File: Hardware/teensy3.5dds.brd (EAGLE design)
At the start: 95.8 x 84.1 mm, 97 parts, among them IC1 AD8034, IC2 AD8034, IC3 AD8034, IC5 AD8034, IC6 AD737KRZ-R7, IC7 AD8034, IC8 AD8034, J1 1776275-2, J2 1776275-2, Q1 10MHz, U1 TEENSY_3.5/3.6_BASIC, U2 ATMEGA32U4-AU, X1 1-227161-0

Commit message: fixes following the advice of people better than me at making PCBs
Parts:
- moved R12 32.3 mm to (49.0, 75.2), turned to 0 degrees
- moved R9 30.7 mm to (48.5, 68.8)
- moved R6 30.1 mm to (49.0, 72.9)
- moved R5 27.7 mm to (43.7, 71.1), turned to 0 degrees
- moved IC1 22.6 mm to (56.4, 72.1)
- moved C1 21.3 mm to (54.6, 77.5)
- moved C2 18.3 mm to (55.1, 68.1), turned to 180 degrees
- moved R11 17.8 mm to (62.5, 73.8), turned to 90 degrees
- moved R13 15.5 mm to (69.0, 78.9), turned to 0 degrees
- moved J_DAC0_OUT 13.6 mm to (53.8, 64.0)
- moved R20 13.5 mm to (63.0, 58.7)
- moved C5 12.7 mm to (68.6, 86.4), turned to 0 degrees
- moved R32 11.3 mm to (63.0, 64.0)
- moved R18 10.5 mm to (45.7, 55.0)
- moved C10 10.5 mm to (52.6, 51.7)
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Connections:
- removed net V-1: R13.1
- net DAC0: now also IC1.5; no longer IC1.3
- net DAC0_OFFSET: now also IC1.1; no longer IC1.7
- net N$21: now also IC1.2; no longer IC1.6
- net N$23: now also IC1.6, IC1.7; no longer IC1.1, IC1.2
- net N$26: now also IC1.3; no longer IC1.5
- net V-: now also R13.1
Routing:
- net V+: track 0.00 -> 409.1 mm, vias 0 -> 15
- net V-: track 68.7 -> 294.1 mm, vias 7 -> 4
- net DAC0_OFFSET: track 83.6 -> 35.0 mm
- net DAC0_SEL: track 70.8 -> 95.1 mm
- net DAC0_OUT: track 0.00 -> 24.0 mm
- net DAC0: track 30.5 -> 49.1 mm
- net SQUARE_SEL: track 120.8 -> 103.6 mm
- net +5V: track 71.3 -> 87.8 mm, vias 4 -> 6
- net N$26: track 12.0 -> 26.5 mm, vias 0 -> 2
- net N$20: track 0.00 -> 13.5 mm
- net N$24: track 3.43 -> 14.9 mm
- net N$14: track 16.1 -> 5.98 mm
- net N$23: track 11.5 -> 4.79 mm
- net SQUARE: track 44.6 -> 38.2 mm
- net N$19: track 40.6 -> 35.3 mm
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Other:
- board size 95.8 x 84.1 mm -> 90 x 84.5 mm

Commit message: board v1.0
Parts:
- removed C30, C34: 100p, rcl:C0805
- removed C32: 10p, rcl:C0805
- removed IC8: AD8034, linear:SO08
- removed J_DAC0_OUT, J_SQUARE_OUT: (no value), con-lstb:MA03-1
- removed J_DISPLAY: (no value), con-lstb:MA04-1
- removed J_SPI: (no value), con-lstb:MA03-2
- removed R43: (no value), rcl:R0805
- removed U$5: (no value), holes:3,0
- added C11, C12: 100n, rcl:C0805
- added C26: 100p, rcl:C0805
- added IC4: AD8034, linear:SO08
- added JDAC0_OUT, JSQUARE_OUT: (no value), con-lstb:MA03-1
- added JDISPLAY: (no value), con-lstb:MA04-1
- added JSPI: (no value), con-lstb:MA03-2
- added R19: 1k, rcl:R0805
- added R21: 787, rcl:M0805
- added R23: 10k, Potentiometer_vertical:MA03-1
- added U$1: (no value), holes:3,0
- C1: value 100n -> 1u; device rcl:C0805 -> rcl:C1206
- C19: device rcl:C1206 -> rcl:C0805
- C22: value 100n -> 10p
- C23: value 1u -> 150p
- C25: value (none) -> 1p
- C27: value 100p -> 10p
- C28: value 10p -> 100p
- C3: value 1u -> 22p; device rcl:C1206 -> rcl:C0805
- C4: value 100n -> 22p
- C5: device rcl:C0805 -> rcl:C1206
- C7: value 22p -> 1u
- C8: value 22p -> 100n
- IC5: value AD8034 -> AD737KRZ-R7; device linear:SO08 -> AD737KRZ-R7:SOIC127P600X175-8N
- IC6: value AD737KRZ-R7 -> AD8034; device AD737KRZ-R7:SOIC127P600X175-8N -> linear:SO08
- Q1: value 10MHz -> 16MHz
- R12: value 1k -> 500; device rcl:R0805 -> rcl:M0805
- R13: value 100k -> 500; device rcl:RTRIM3296W -> rcl:M0805
- R15: value (none) -> 2.74k
- R16: value (none) -> 100k; device rcl:M0805 -> rcl:RTRIM3296W
- R17: value (none) -> 1k; device rcl:M0805 -> rcl:R0805
- R18: value 2.74k -> 1k
- R20: value 787 -> 1k; device rcl:M0805 -> rcl:R0805
- R22: value 14.3k -> 1k; device rcl:M0805 -> rcl:R0805
- R25: value 10k -> 1.5k; device Potentiometer_vertical:MA03-1 -> rcl:R0805
- R26: value (none) -> 14.3k; device rcl:R0805 -> rcl:M0805
- R27, R42: value (none) -> 50
- R28, R37: value (none) -> 5k
- R30, R41: value (none) -> 1k
- R31: value 10k -> 2k; device Potentiometer_vertical:MA03-1 -> rcl:M0805
- R32: value 562 -> 10k; device rcl:R0805 -> Potentiometer_vertical:MA03-1
- R33: value 243 -> 10k
- R34: value 20k -> 562
- R35: value 1.78k -> (none); device rcl:M0805 -> rcl:R0805
- R36: value (none) -> 20k
- R38: value (none) -> 10k
- R39: value (none) -> 14.3k
- R4, R9: value 1k -> 10k
- R40: value 50 -> (none)
- R5: value 100k -> 10k; device rcl:RTRIM3296W -> rcl:R0805
- R6: value 1k -> 100k; device rcl:R0805 -> rcl:RTRIM3296W
- RL1, RL2: value PRME_15005SOCKET -> PRME_15005NOSOCKET; device prme15005:DIL14_SOCKET -> prme15005:DIL14
- moved R15 89.0 mm to (2.92, 59.8), turned to 0 degrees
- moved J2 86.6 mm to (84.6, 92.7)
- moved J1 80.3 mm to (84.6, 81.8)
- moved R41 79.2 mm to (78.7, 54.9), turned to 180 degrees
- moved R10 78.9 mm to (3.05, 71.4)
- moved C13 78.4 mm to (2.92, 55.2), turned to 0 degrees
- moved X1 77.2 mm to (7.37, 46.2)
- moved R1 74.2 mm to (86.2, 54.3)
- moved LED1 74.1 mm to (85.5, 52.0)
- moved R8 73.8 mm to (3.05, 69.2), turned to 0 degrees
- moved C19 72.5 mm to (67.9, 45.1), turned to 0 degrees
- moved S1 71.3 mm to (79.9, 40.4)
- moved R35 70.9 mm to (17.0, 49.5), turned to 0 degrees
- moved C18 67.0 mm to (78.7, 59.7), turned to 0 degrees
- moved R7 66.7 mm to (16.5, 72.6)
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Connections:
- removed net N$20: R13.2, R4.1
- new net N$36: IC6.2, R35.2, R40.1
- new net N$37: IC7.6, R16.2, R18.1
- net +5V: now also C1.1, C2.1, C5.1, C7.1, JDISPLAY.3, JSPI.5, R4.1, R5.1; no longer C19.1, C22.1, C23.1, C3.1, J_DISPLAY.3, J_SPI.5, R41.1, R42.1
- net AMPL_MEASURE: now also IC4.7, R41.2, U2.37; no longer IC5.7, R39.2, U2.38
- net DAC0_FILTERED: now also C28.1, JDAC0_OUT.1; no longer C34.1, J_DAC0_OUT.1
- net DAC0_OFFSET: now also JDAC0_OUT.3, R11.1; no longer J_DAC0_OUT.3, R12.1
- net DAC0_OUT: now also JDAC0_OUT.2; no longer J_DAC0_OUT.2
- net DAC0_SEL: now also R13.1, U1.22/A8; no longer R17.1, U1.36/A17
- net GND: now also C10.2, C11.1, C12.2, C13.1, C14.2, C15.1, C16.2, C17.1, C18.2, C19.1, C2.2, C22.1, C27.1, C3.1, C4.1, C5.2, C7.2, C8.2, C9.1, IC5.3, IC5.8, JDISPLAY.4, JSPI.1, R10.2, R19.2, R9.1; no longer C10.1, C13.2, C14.1, C15.2, C16.1, C17.2, C18.1, C19.2, C2.1, C22.2, C23.2, C28.1, C3.2, C32.1, C4.2, C5.1, C7.1, C8.1, C9.2, IC6.8, IC7.6, J_DISPLAY.4, J_SPI.1, R43.1, R6.2, R8.2
- net INTERRUPT: now also U1.21/A7, U2.22; no longer U1.37/A18, U2.25
- net MISO: now also JSPI.3; no longer J_SPI.3
- net MOSI: now also JSPI.6; no longer J_SPI.6
- net N$1: now also R31.2, R33.1; no longer R33.2, R35.1
- net N$10: now also R22.1; no longer R24.1
- net N$11: now also IC4.2; no longer IC5.2
- net N$13: now also IC4.3, R24.1, R25.2; no longer IC5.3, R26.1, R27.2
- net N$14: now also IC5.6, R37.1; no longer IC6.6, R36.1
- net N$15: now also R32.1; no longer R31.1
- net N$16: now also IC4.6, R37.2, R41.1; no longer IC5.6, R36.2, R39.1
- net N$17: now also R12.2; no longer R16.2
- net N$18: now also R13.2; no longer R17.2
- net N$19: now also IC6.1, R40.2, R42.1; no longer IC8.1, IC8.2, R40.1
- net N$21: now also R10.1, R11.2; no longer R12.2, R6.1
- net N$22: now also IC4.5, R38.2, R39.1; no longer IC5.5, R37.2, R38.1
- net N$23: now also R7.1; no longer R11.1
- net N$24: now also R19.1, R20.2; no longer R10.2, R8.1
- net N$25: now also R4.2, U2.40; no longer R41.2, U2.32
- net N$26: now also R7.2, R8.2; no longer R11.2, R9.2
- net N$27: now also R17.1; no longer R7.1
- net N$28: now also R17.2, R18.2; no longer R4.2, R7.2
- net N$29: now also R9.2, U2.39; no longer R43.2, U2.30
- net N$3: now also IC6.5, R23.2; no longer IC8.5, R25.2
- net N$31: now also C3.2; no longer C7.2
- net N$34: now also R27.1, R31.1; no longer R15.1, R33.1
- net N$4: now also C4.2; no longer C8.2
- net N$5: now also IC6.6, R22.2; no longer IC8.6, R24.2
- net N$50: now also C23.2, R15.1; no longer C27.2, R18.1
- net N$53: now also C23.1, R21.1; no longer C27.1, R20.1
- net N$56: now also R6.2, R8.1; no longer R5.2, R9.1
- net N$58: now also C22.2, R15.2; no longer C24.2, R18.2
- net N$6: now also R42.2; no longer R40.2
- net N$61: now also C26.1, R21.2, R26.1; no longer C30.1, R20.2, R22.1
- net N$62: now also C26.2, R34.1; no longer C30.2, R32.1
- net N$63: now also C24.2, R26.2; no longer C28.2, R22.2
- net N$73: now also C28.2, R34.2, R36.1; no longer C34.2, R32.2, R34.1
- net N$75: now also C27.2, R36.2; no longer C32.2, R34.2
- net N$8: now also R5.2, U2.41; no longer R42.2, U2.31
- net N$9: now also IC5.2, IC6.7, R32.2, R32.3, R35.1; no longer IC6.2, IC8.3, IC8.7, R31.2, R31.3
- net OFF_MEASURE: now also IC4.1, U2.36; no longer IC5.1, U2.37
- net RX1: now also U1.1/TX; no longer U1.32/A13
- net SCK: now also JSPI.4; no longer J_SPI.4
- net SCL: now also JDISPLAY.1; no longer J_DISPLAY.1
- net SDA: now also JDISPLAY.2; no longer J_DISPLAY.2
- net SQUARE: now also U1.A22/DAC1; no longer U1.39/A20
- net SQUARE_FILTERED: now also JSQUARE_OUT.1, R33.2; no longer J_SQUARE_OUT.1, R35.2
- net SQUARE_OFFSET: now also JSQUARE_OUT.3, R20.1, R27.2; no longer J_SQUARE_OUT.3, R10.1, R15.2
- net SQUARE_OUT: now also JSQUARE_OUT.2; no longer J_SQUARE_OUT.2
- net SQUARE_SEL: now also R12.1, U1.23/A9; no longer R16.1, U1.35/A16
- net SS: now also JSPI.2; no longer J_SPI.2
- net TX1: now also U1.0/RX; no longer U1.31/A12
- net V+: now also C10.1, C12.1, C14.1, C16.1, C18.1, C8.1, IC4.8, IC5.7, IC6.8, R16.3, R23.3, R24.2, R38.1, R6.3; no longer C1.1, C13.1, C15.1, C17.1, C4.1, C9.1, IC5.8, IC6.7, IC8.8, R13.3, R25.3, R26.2, R37.1, R5.3
- net V-: now also C11.2, C13.2, C15.2, C17.2, C19.2, C9.2, IC4.4, IC5.5, R16.1, R23.1, R39.2, R6.1; no longer C10.2, C14.2, C16.2, C18.2, C2.2, C5.2, IC6.5, IC8.4, R13.1, R27.1, R38.2, R5.1
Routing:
- net SQUARE_SEL: track 103.6 -> 20.4 mm
- net V-: track 294.1 -> 372.0 mm, vias 4 -> 7
- net DAC0_SEL: track 95.1 -> 40.3 mm, vias 1 -> 3
- net INTERRUPT: track 77.7 -> 27.4 mm
- net V+: track 409.1 -> 447.7 mm, vias 15 -> 11
- net +5V: track 87.8 -> 50.2 mm, vias 6 -> 11
- net N$14: track 5.98 -> 41.1 mm, vias 0 -> 2
- net N$37: track 0.00 -> 34.9 mm, vias 0 -> 2
- net AMPL_MEASURE: track 47.2 -> 15.7 mm, vias 2 -> 0
- net DAC0: track 49.1 -> 18.6 mm
- net DAC0_OFFSET: track 35.0 -> 65.4 mm, vias 2 -> 1
- net SQUARE_OFFSET: track 58.6 -> 29.2 mm, vias 1 -> 0
- net N$9: track 65.4 -> 39.0 mm
- net N$10: track 16.5 -> 41.7 mm, vias 0 -> 1
- net N$8: track 68.9 -> 44.5 mm
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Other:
- board size 90 x 84.5 mm -> 90.4 x 63.4 mm
- board text added: "vcc"

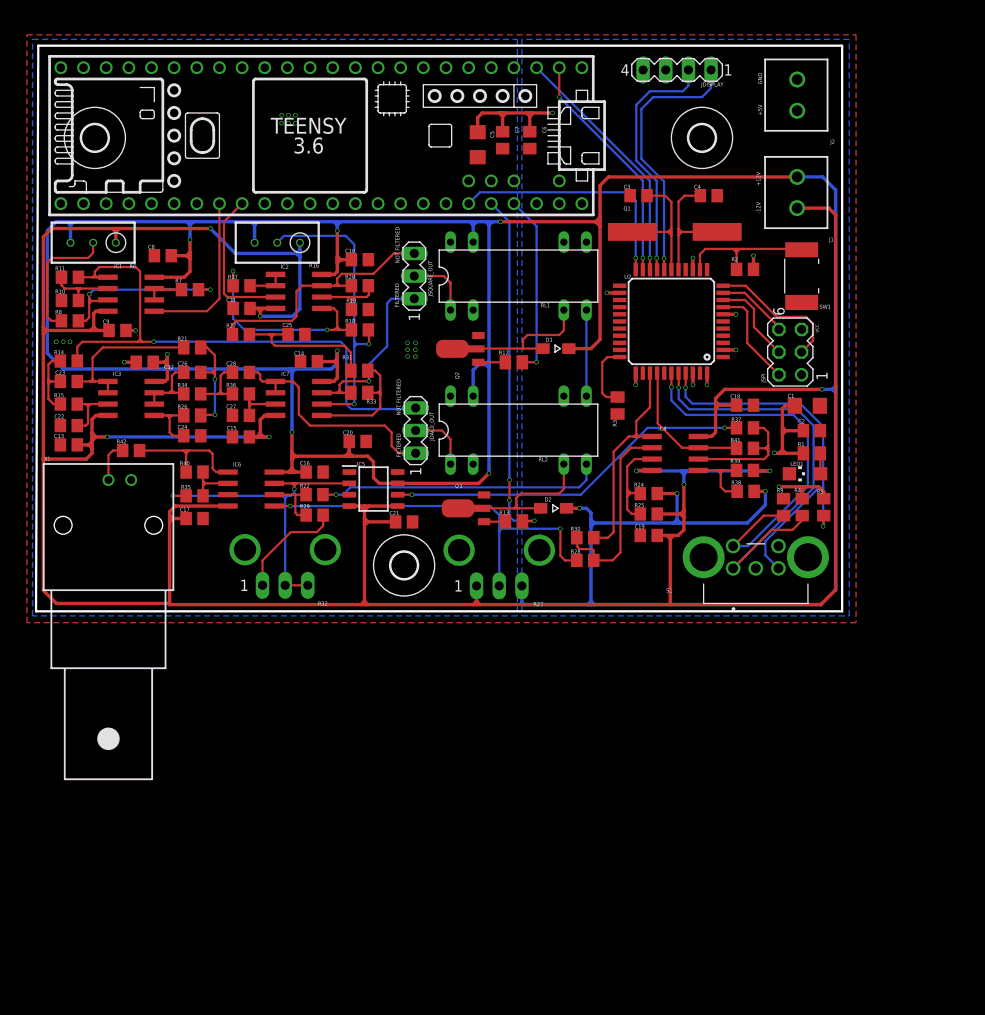
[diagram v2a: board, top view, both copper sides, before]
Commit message: hardware: board v2.0
correct a few derps with missing resistors
correct encoder pushbutton
add i2c pullup resistors
move some 32u4 pins to more accessible ones, supported by the arduino micro bootloader
wire the 5v led to the builtin led on 32u4
remove the ad737, move the a non-inverting summer circuit (wave+offset) with a peak finder to get the peak of the wave no matter the offset condition
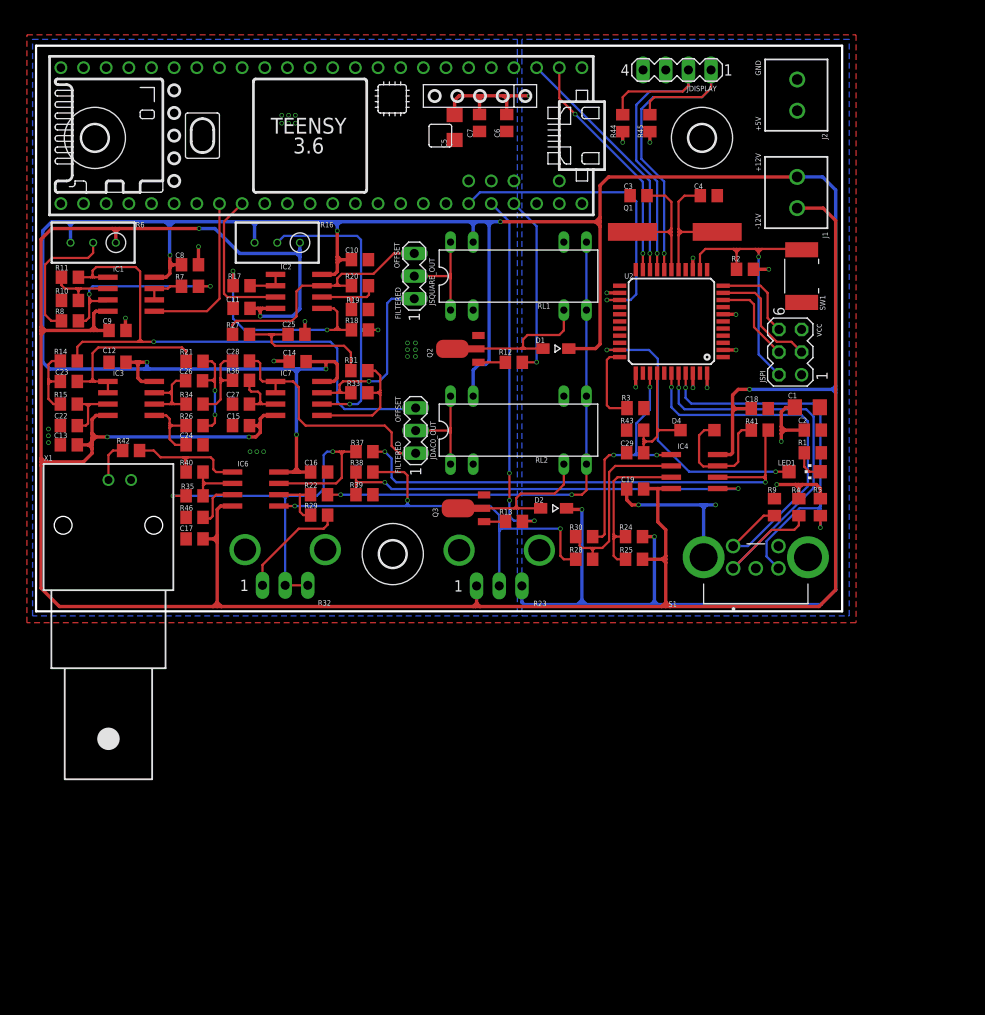
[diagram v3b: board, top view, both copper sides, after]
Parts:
- removed C20, C21: 100n, rcl:C0805
- removed IC5: AD737KRZ-R7, AD737KRZ-R7:SOIC127P600X175-8N
- added C29: (no value), rcl:C0805
- added D4: (no value), diode:SOD123
- added R43, R44, R45, R46: (no value), rcl:R0805
- C1: value 1u -> 100u
- C5: value 100n -> 100u
- C7: value 1u -> 100n
- R1, R12, R13, R21, R26, R31, R33: device rcl:M0805 -> rcl:R0805
- moved R38 42.8 mm to (36.1, 52.2)
- moved R39 42.8 mm to (36.1, 49.7)
- moved R37 42.8 mm to (36.1, 54.5)
- moved C19 5.43 mm to (66.4, 50.3)
- moved R25 5.34 mm to (66.3, 42.4)
- moved R24 5.10 mm to (66.3, 45.0)
- moved C5 3.23 mm to (46.2, 90.8)
- moved C6 3.23 mm to (52.0, 91.3)
- moved C7 3.23 mm to (49.0, 91.3)
- moved C8 3.21 mm to (16.5, 75.4), turned to 0 degrees
- moved C12 3.05 mm to (8.38, 64.5)
- moved IC4 2.96 mm to (73.1, 52.3)
- moved R41 2.62 mm to (80.4, 56.9)
- moved C17 2.29 mm to (17.0, 44.7), turned to 0 degrees
- moved R3 2.03 mm to (66.5, 59.4), turned to 0 degrees
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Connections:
- removed net N$14 (its old number): IC5.6, R37.1
- removed net N$35: R2.1, SW1.P$2, U2.13
- removed net SS: JSPI.2, U2.8
- new net N$20: D4.A, IC4.7, R41.2
- new net N$22: IC6.3, R46.2
- new net N$38: LED1.C, R1.2
- new net RST: JSPI.2, R2.1, SW1.P$2, U2.13
- net +5V: now also R44.2, R45.1, S1.4; no longer R1.2
- net AMPL_MEASURE: now also C29.1, D4.C, R43.2; no longer IC4.7, R41.2
- net GND: now also C29.2, R1.1, R39.2, R43.1, R46.1; no longer C20.2, C21.1, IC5.3, IC5.8, IC6.3, LED1.C, S1.4
- net INTERRUPT: now also U2.25; no longer U2.22
- net MISO: now also JSPI.6; no longer JSPI.3
- net MOSI: now also JSPI.3; no longer JSPI.6
- net N$3: now also R38.1
- net N$30: now also U2.32; no longer R1.1
- net N$9: now also R37.1; no longer IC5.2
- net SCL: now also R45.2
- net SDA: now also R44.1
- net V+: no longer C20.1, IC5.7, R38.1
- net V-: no longer C21.2, IC5.4, IC5.5, R39.2
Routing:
- net V+: track 447.7 -> 378.8 mm, vias 11 -> 9
- net V-: track 372.0 -> 324.2 mm, vias 7 -> 4
- net N$16: track 15.0 -> 58.6 mm, vias 0 -> 2
- net N$14 (its old number): track 41.1 -> 0.00 mm, vias 2 -> 0
- net N$14: track 9.05 -> 48.6 mm, vias 0 -> 2
- net RST: track 0.00 -> 32.9 mm, vias 0 -> 1
- net N$30: track 2.30 -> 32.9 mm, vias 0 -> 2
- net GND: track 2.41 -> 24.8 mm, vias 17 -> 24
- net N$35: track 16.8 -> 0.00 mm
- net N$10: track 41.7 -> 57.1 mm, vias 1 -> 2
- net N$20: track 0.00 -> 14.6 mm
- net SDA: track 28.0 -> 39.6 mm
- net N$9: track 39.0 -> 50.5 mm
- net SS: track 11.5 -> 0.00 mm
- net SCL: track 29.9 -> 40.9 mm
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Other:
- outline, holes or cut-outs redrawn
- board text added: "JLCJLCJLCJLC"
- board text added: "OFFSET"
- board text added: "Teensy 3.5 DDS Signal Generator by EmaMaker - https://github.com/EmaMaker/SignalGenerator-Teensy"
- board text removed: "NOT FILTERED"
